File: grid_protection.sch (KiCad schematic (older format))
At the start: 10 parts, among them U2 74HC14, U6 NE555D, U7 74HC08

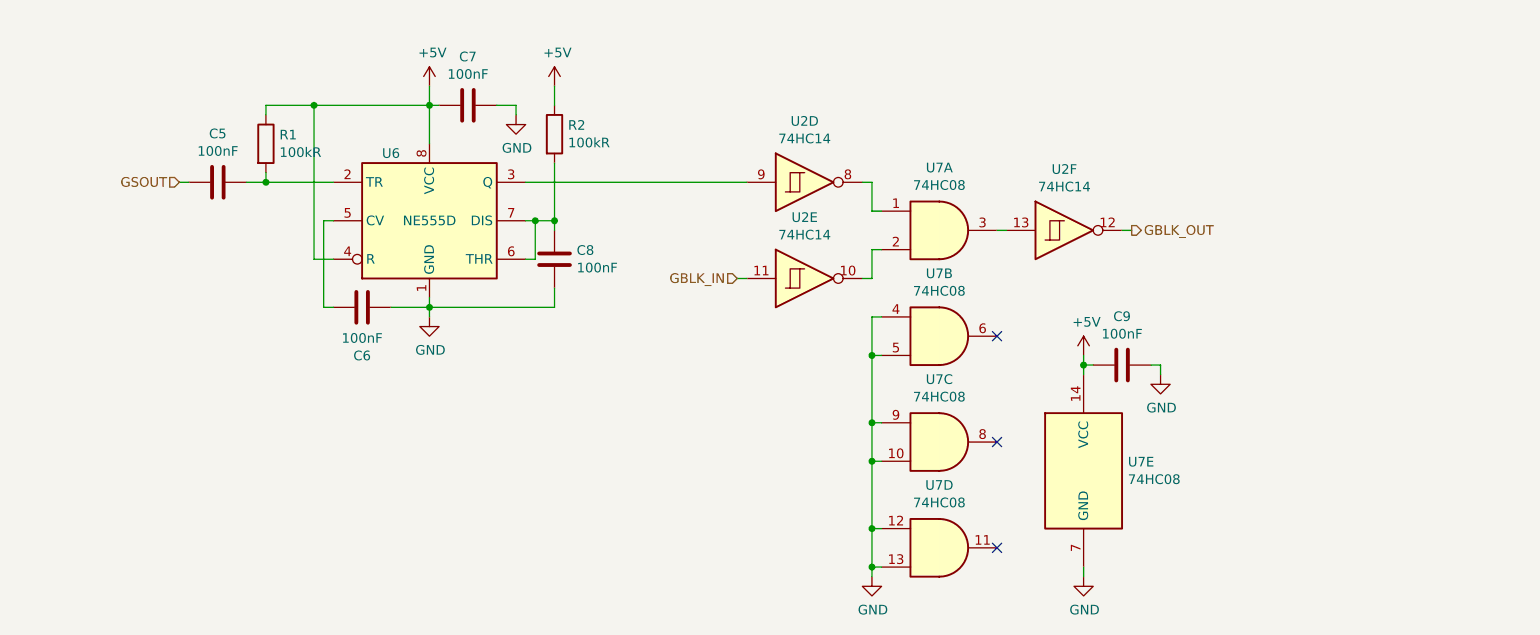
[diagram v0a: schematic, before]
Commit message: Connect shutdown and ifsel
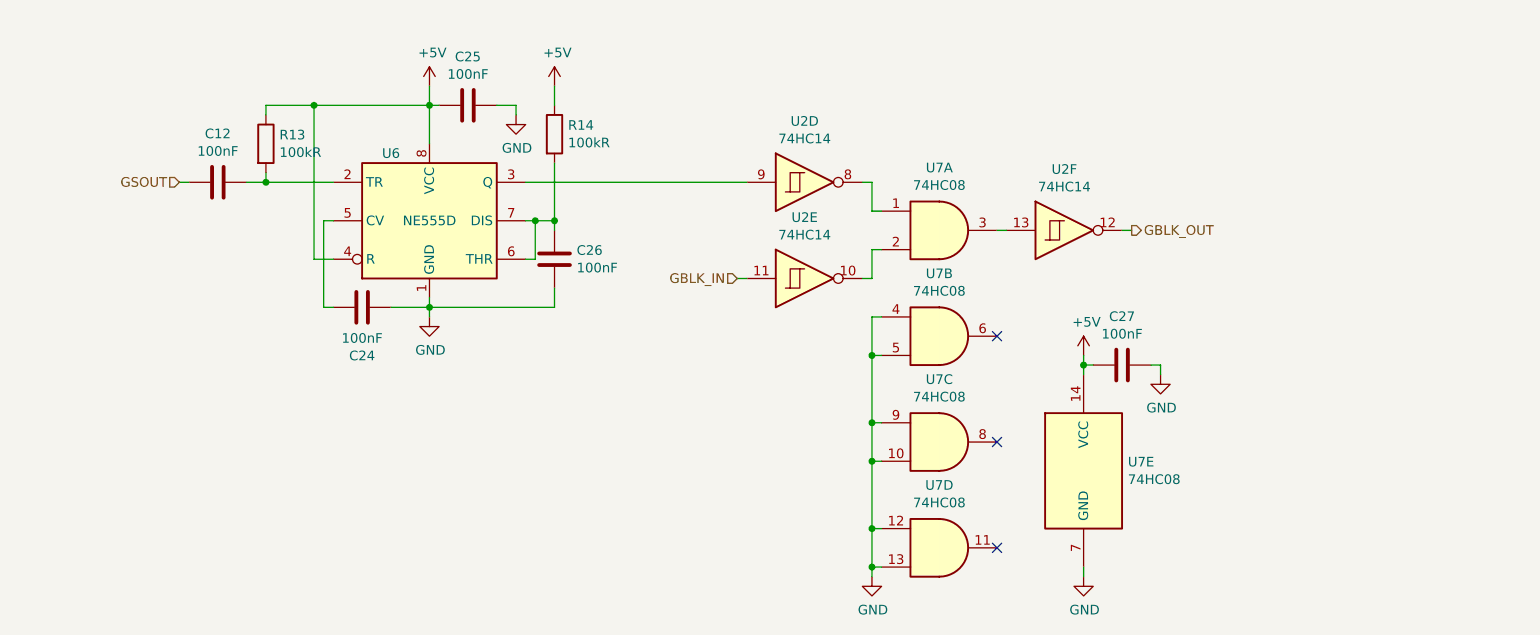
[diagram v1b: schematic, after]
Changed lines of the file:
@@
 $Descr A4 11693 8268
 encoding utf-8
-Sheet 2 4
+Sheet 4 6
 Title ""
 Date ""
@@
 AR Path="/5FBC6E69" Ref="C?"  Part="1"
 AR Path="/5FBBCA4E/5FBC6E69" Ref="C5"  Part="1"
-F 0 "C5" V 1448 3300 50  0000 C CNN
+AR Path="/60B03476/60B1C00D/5FBC6E69" Ref="C12"  Part="1"
+F 0 "C12" V 1448 3300 50  0000 C CNN
 F 1 "100nF" V 1539 3300 50  0000 C CNN
 F 2 "Capacitor_SMD:C_0402_1005Metric" H 1738 3150 50  0001 C CNN
@@
 U 1 1 5FBC8F6E
 P 2800 4000
-F 0 "#PWR014" H 2800 3750 50  0001 C CNN
+AR Path="/5FBBCA4E/5FBC8F6E" Ref="#PWR014"  Part="1"
+AR Path="/60B03476/60B1C00D/5FBC8F6E" Ref="#PWR0143"  Part="1"
+F 0 "#PWR0143" H 2800 3750 50  0001 C CNN
 F 1 "GND" H 2805 3827 50  0000 C CNN
 F 2 "" H 2800 4000 50  0001 C CNN
@@
 U 1 1 5FBC9E40
 P 3250 2950
-F 0 "#PWR015" H 3250 2700 50  0001 C CNN
+AR Path="/5FBBCA4E/5FBC9E40" Ref="#PWR015"  Part="1"
+AR Path="/60B03476/60B1C00D/5FBC9E40" Ref="#PWR0144"  Part="1"
+F 0 "#PWR0144" H 3250 2700 50  0001 C CNN
 F 1 "GND" H 3255 2777 50  0000 C CNN
 F 2 "" H 3250 2950 50  0001 C CNN
@@
 U 1 1 5FBCADA0
 P 2800 2800
-F 0 "#PWR013" H 2800 2650 50  0001 C CNN
+AR Path="/5FBBCA4E/5FBCADA0" Ref="#PWR013"  Part="1"
+AR Path="/60B03476/60B1C00D/5FBCADA0" Ref="#PWR0145"  Part="1"
+F 0 "#PWR0145" H 2800 2650 50  0001 C CNN
 F 1 "+5V" H 2815 2973 50  0000 C CNN
 F 2 "" H 2800 2800 50  0001 C CNN
@@
 AR Path="/5FBCDE60" Ref="C?"  Part="1"
 AR Path="/5FBBCA4E/5FBCDE60" Ref="C6"  Part="1"
-F 0 "C6" V 2198 3950 50  0000 C CNN
+AR Path="/60B03476/60B1C00D/5FBCDE60" Ref="C24"  Part="1"
+F 0 "C24" V 2198 3950 50  0000 C CNN
 F 1 "100nF" V 2289 3950 50  0000 C CNN
 F 2 "Capacitor_SMD:C_0402_1005Metric" H 2488 3800 50  0001 C CNN
@@
 AR Path="/5FBD22E7" Ref="C?"  Part="1"
 AR Path="/5FBBCA4E/5FBD22E7" Ref="C8"  Part="1"
-F 0 "C8" H 3565 3746 50  0000 L CNN
+AR Path="/60B03476/60B1C00D/5FBD22E7" Ref="C26"  Part="1"
+F 0 "C26" H 3565 3746 50  0000 L CNN
 F 1 "100nF" H 3565 3655 50  0000 L CNN
 F 2 "Capacitor_SMD:C_0402_1005Metric" H 3488 3550 50  0001 C CNN
@@
 U 1 1 5FBD37F0
 P 3450 3050
-F 0 "R2" H 3520 3096 50  0000 L CNN
+AR Path="/5FBBCA4E/5FBD37F0" Ref="R2"  Part="1"
+AR Path="/60B03476/60B1C00D/5FBD37F0" Ref="R14"  Part="1"
+F 0 "R14" H 3520 3096 50  0000 L CNN
 F 1 "100kR" H 3520 3005 50  0000 L CNN
 F 2 "Resistor_SMD:R_0402_1005Metric" V 3380 3050 50  0001 C CNN
@@
 U 1 1 5FBD7446
 P 3450 2800
-F 0 "#PWR016" H 3450 2650 50  0001 C CNN
+AR Path="/5FBBCA4E/5FBD7446" Ref="#PWR016"  Part="1"
+AR Path="/60B03476/60B1C00D/5FBD7446" Ref="#PWR0146"  Part="1"
+F 0 "#PWR0146" H 3450 2650 50  0001 C CNN
 F 1 "+5V" H 3465 2973 50  0000 C CNN
 F 2 "" H 3450 2800 50  0001 C CNN
@@
 U 1 1 5FBD921F
 P 1950 3100
-F 0 "R1" H 2020 3146 50  0000 L CNN
+AR Path="/5FBBCA4E/5FBD921F" Ref="R1"  Part="1"
+AR Path="/60B03476/60B1C00D/5FBD921F" Ref="R13"  Part="1"
+F 0 "R13" H 2020 3146 50  0000 L CNN
 F 1 "100kR" H 2020 3055 50  0000 L CNN
 F 2 "Resistor_SMD:R_0402_1005Metric" V 1880 3100 50  0001 C CNN
@@
 AR Path="/5FBC9A76" Ref="C?"  Part="1"
 AR Path="/5FBBCA4E/5FBC9A76" Ref="C7"  Part="1"
-F 0 "C7" V 2748 2900 50  0000 C CNN
+AR Path="/60B03476/60B1C00D/5FBC9A76" Ref="C25"  Part="1"
+F 0 "C25" V 2748 2900 50  0000 C CNN
 F 1 "100nF" V 2839 2900 50  0000 C CNN
 F 2 "Capacitor_SMD:C_0402_1005Metric" H 3038 2750 50  0001 C CNN
@@
 AR Path="/5FC1C26C" Ref="U?"  Part="4"
 AR Path="/5FBBCA4E/5FC1C26C" Ref="U7"  Part="4"
+AR Path="/60B03476/60B1C00D/5FC1C26C" Ref="U7"  Part="4"
 F 0 "U7" H 5450 5525 50  0000 C CNN
 F 1 "74HC08" H 5450 5434 50  0000 C CNN
@@
 AR Path="/5FC1C27D" Ref="C?"  Part="1"
 AR Path="/5FBBCA4E/5FC1C27D" Ref="C9"  Part="1"
-F 0 "C9" V 6148 4250 50  0000 C CNN
+AR Path="/60B03476/60B1C00D/5FC1C27D" Ref="C27"  Part="1"
+F 0 "C27" V 6148 4250 50  0000 C CNN
 F 1 "100nF" V 6239 4250 50  0000 C CNN
 F 2 "Capacitor_SMD:C_0402_1005Metric" H 6438 4100 50  0001 C CNN
@@
 AR Path="/5FC1C283" Ref="#PWR?"  Part="1"
 AR Path="/5FBBCA4E/5FC1C283" Ref="#PWR020"  Part="1"
-F 0 "#PWR020" H 6600 4050 50  0001 C CNN
+AR Path="/60B03476/60B1C00D/5FC1C283" Ref="#PWR0147"  Part="1"
+F 0 "#PWR0147" H 6600 4050 50  0001 C CNN
 F 1 "GND" H 6605 4127 50  0000 C CNN
 F 2 "" H 6600 4300 50  0001 C CNN
@@
 AR Path="/5FC1C28D" Ref="#PWR?"  Part="1"
 AR Path="/5FBBCA4E/5FC1C28D" Ref="#PWR018"  Part="1"
-F 0 "#PWR018" H 6200 4050 50  0001 C CNN
+AR Path="/60B03476/60B1C00D/5FC1C28D" Ref="#PWR0148"  Part="1"
+F 0 "#PWR0148" H 6200 4050 50  0001 C CNN
 F 1 "+5V" H 6215 4373 50  0000 C CNN
 F 2 "" H 6200 4200 50  0001 C CNN
@@
 AR Path="/5FC1C295" Ref="#PWR?"  Part="1"
 AR Path="/5FBBCA4E/5FC1C295" Ref="#PWR019"  Part="1"
-F 0 "#PWR019" H 6200 5100 50  0001 C CNN
+AR Path="/60B03476/60B1C00D/5FC1C295" Ref="#PWR0149"  Part="1"
+F 0 "#PWR0149" H 6200 5100 50  0001 C CNN
 F 1 "GND" H 6205 5177 50  0000 C CNN
 F 2 "" H 6200 5350 50  0001 C CNN
@@
 AR Path="/5FC1C29E" Ref="#PWR?"  Part="1"
 AR Path="/5FBBCA4E/5FC1C29E" Ref="#PWR017"  Part="1"
-F 0 "#PWR017" H 5100 5100 50  0001 C CNN
+AR Path="/60B03476/60B1C00D/5FC1C29E" Ref="#PWR0150"  Part="1"
+F 0 "#PWR0150" H 5100 5100 50  0001 C CNN
 F 1 "GND" H 5105 5177 50  0000 C CNN
 F 2 "" H 5100 5350 50  0001 C CNN
@@
 AR Path="/5FC1C273" Ref="U?"  Part="5"
 AR Path="/5FBBCA4E/5FC1C273" Ref="U7"  Part="5"
+AR Path="/60B03476/60B1C00D/5FC1C273" Ref="U7"  Part="5"
 F 0 "U7" H 6430 4846 50  0000 L CNN
 F 1 "74HC08" H 6430 4755 50  0000 L CNN
@@
 AR Path="/5FC1C265" Ref="U?"  Part="3"
 AR Path="/5FBBCA4E/5FC1C265" Ref="U7"  Part="3"
+AR Path="/60B03476/60B1C00D/5FC1C265" Ref="U7"  Part="3"
 F 0 "U7" H 5450 4975 50  0000 C CNN
 F 1 "74HC08" H 5450 4884 50  0000 C CNN
@@
 AR Path="/5FC1C25E" Ref="U?"  Part="2"
 AR Path="/5FBBCA4E/5FC1C25E" Ref="U7"  Part="2"
+AR Path="/60B03476/60B1C00D/5FC1C25E" Ref="U7"  Part="2"
 F 0 "U7" H 5450 4425 50  0000 C CNN
 F 1 "74HC08" H 5450 4334 50  0000 C CNN
@@
 AR Path="/5FBBEE91" Ref="U?"  Part="5"
 AR Path="/5FBBCA4E/5FBBEE91" Ref="U2"  Part="5"
+AR Path="/60B03476/60B1C00D/5FBBEE91" Ref="U2"  Part="5"
 F 0 "U2" H 4750 4117 50  0000 C CNN
 F 1 "74HC14" H 4750 4026 50  0000 C CNN
@@
 AR Path="/5FBBEE8A" Ref="U?"  Part="6"
 AR Path="/5FBBCA4E/5FBBEE8A" Ref="U2"  Part="6"
+AR Path="/60B03476/60B1C00D/5FBBEE8A" Ref="U2"  Part="6"
 F 0 "U2" H 6100 3867 50  0000 C CNN
 F 1 "74HC14" H 6100 3776 50  0000 C CNN
@@
 AR Path="/5FBBEE83" Ref="U?"  Part="1"
 AR Path="/5FBBCA4E/5FBBEE83" Ref="U7"  Part="1"
+AR Path="/60B03476/60B1C00D/5FBBEE83" Ref="U7"  Part="1"
 F 0 "U7" H 5450 3875 50  0000 C CNN
 F 1 "74HC08" H 5450 3784 50  0000 C CNN
@@
 AR Path="/5FBBEE98" Ref="U?"  Part="4"
 AR Path="/5FBBCA4E/5FBBEE98" Ref="U2"  Part="4"
+AR Path="/60B03476/60B1C00D/5FBBEE98" Ref="U2"  Part="4"
 F 0 "U2" H 4750 3617 50  0000 C CNN
 F 1 "74HC14" H 4750 3526 50  0000 C CNN
@@
 U 1 1 5FCFCDB6
 P 2800 3500
+AR Path="/5FBBCA4E/5FCFCDB6" Ref="U6"  Part="1"
+AR Path="/60B03476/60B1C00D/5FCFCDB6" Ref="U6"  Part="1"
 F 0 "U6" H 2600 3850 50  0000 C CNN
 F 1 "NE555D" H 2800 3500 50  0000 C CNN

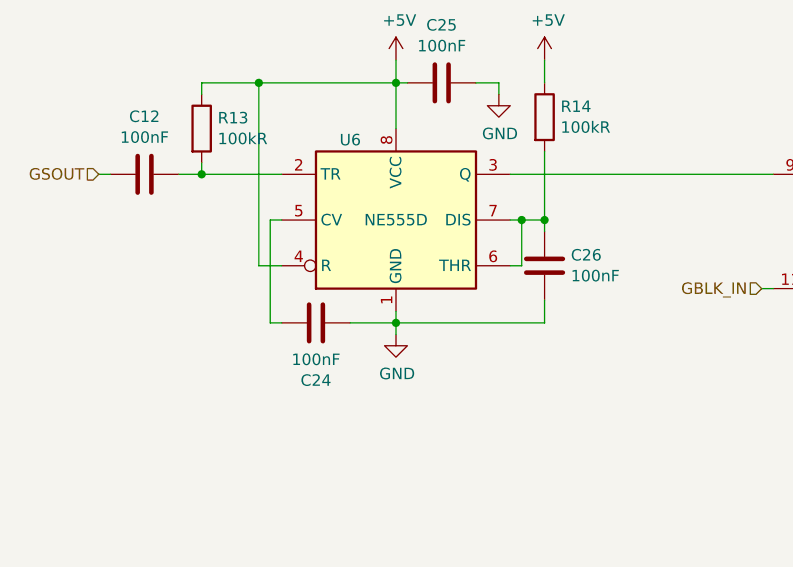
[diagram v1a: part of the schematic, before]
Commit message: Add VFD section
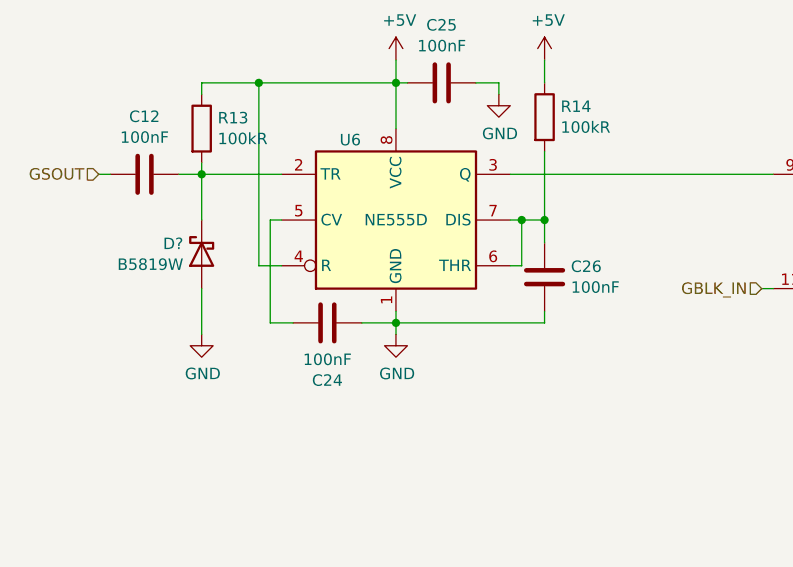
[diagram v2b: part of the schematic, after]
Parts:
- added D?: B5819W, Diode_SMD:D_SOD-123, symbol Device:D_Schottky
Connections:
- net GND: now also D?.2 (A)
- net at C5.1, R1.2, U6.2 (TR): now also D?.1 (K)
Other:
- moved on the sheet: C24, C26
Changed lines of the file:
@@
 $Descr A4 11693 8268
 encoding utf-8
-Sheet 4 6
+Sheet 4 7
 Title ""
 Date ""
@@
 L Device:C C?
 U 1 1 5FBCDE60
-P 2450 3950
+P 2500 3950
 AR Path="/5FBCDE60" Ref="C?"  Part="1"
 AR Path="/5FBBCA4E/5FBCDE60" Ref="C6"  Part="1"
 AR Path="/60B03476/60B1C00D/5FBCDE60" Ref="C24"  Part="1"
-F 0 "C24" V 2198 3950 50  0000 C CNN
-F 1 "100nF" V 2289 3950 50  0000 C CNN
-F 2 "Capacitor_SMD:C_0402_1005Metric" H 2488 3800 50  0001 C CNN
-F 3 "~" H 2450 3950 50  0001 C CNN
-F 4 "C1525" V 2450 3950 50  0001 C CNN "LCSC"
-	1    2450 3950
+F 0 "C24" V 2248 3950 50  0000 C CNN
+F 1 "100nF" V 2339 3950 50  0000 C CNN
+F 2 "Capacitor_SMD:C_0402_1005Metric" H 2538 3800 50  0001 C CNN
+F 3 "~" H 2500 3950 50  0001 C CNN
+F 4 "C1525" V 2500 3950 50  0001 C CNN "LCSC"
+	1    2500 3950
 	0    -1   -1   0
 $EndComp
 Wire Wire Line
 	2800 3900 2800 3950
-Wire Wire Line
-	2800 3950 2600 3950
 Connection ~ 2800 3950
 Wire Wire Line
 	2800 3950 2800 4000
-Wire Wire Line
-	2300 3950 2250 3950
 Wire Wire Line
 	1850 3300 1950 3300
@@
 L Device:C C?
 U 1 1 5FBD22E7
-P 3450 3700
+P 3450 3750
 AR Path="/5FBD22E7" Ref="C?"  Part="1"
 AR Path="/5FBBCA4E/5FBD22E7" Ref="C8"  Part="1"
 AR Path="/60B03476/60B1C00D/5FBD22E7" Ref="C26"  Part="1"
-F 0 "C26" H 3565 3746 50  0000 L CNN
-F 1 "100nF" H 3565 3655 50  0000 L CNN
-F 2 "Capacitor_SMD:C_0402_1005Metric" H 3488 3550 50  0001 C CNN
-F 3 "~" H 3450 3700 50  0001 C CNN
-F 4 "C1525" V 3450 3700 50  0001 C CNN "LCSC"
-	1    3450 3700
+F 0 "C26" H 3565 3796 50  0000 L CNN
+F 1 "100nF" H 3565 3705 50  0000 L CNN
+F 2 "Capacitor_SMD:C_0402_1005Metric" H 3488 3600 50  0001 C CNN
+F 3 "~" H 3450 3750 50  0001 C CNN
+F 4 "C1525" V 3450 3750 50  0001 C CNN "LCSC"
+	1    3450 3750
 	1    0    0    -1
 $EndComp
@@
 	3450 3500 3450 3200
 Connection ~ 3350 3500
-Wire Wire Line
-	3450 3500 3450 3550
 Connection ~ 3450 3500
-Wire Wire Line
-	3450 3950 3450 3850
 Wire Wire Line
 	2800 3950 3450 3950
@@
 	1    0    0    -1
 $EndComp
+$Comp
+L Device:D_Schottky D?
+U 1 1 6188A910
+P 1950 3650
+AR Path="/60B03476/60B1C0DE/6188A910" Ref="D?"  Part="1"
+AR Path="/60B03476/60B1C0E2/6188A910" Ref="D?"  Part="1"
+AR Path="/60B03476/6147410E/6188A910" Ref="D?"  Part="1"
+AR Path="/60B03476/60B1C00D/6188A910" Ref="D?"  Part="1"
+F 0 "D?" V 1904 3730 50  0000 L CNN
+F 1 "B5819W" V 1995 3730 50  0000 L CNN
+F 2 "Diode_SMD:D_SOD-123" H 1950 3650 50  0001 C CNN
+F 3 "~" H 1950 3650 50  0001 C CNN
+F 4 "C8598" H 1950 3650 50  0001 C CNN "LCSC"
+	1    1950 3650
+	0    -1   1    0
+$EndComp
+$Comp
+L power:GND #PWR?
+U 1 1 6188C155
+P 1950 4000
+F 0 "#PWR?" H 1950 3750 50  0001 C CNN
+F 1 "GND" H 1955 3827 50  0000 C CNN
+F 2 "" H 1950 4000 50  0001 C CNN
+F 3 "" H 1950 4000 50  0001 C CNN
+	1    1950 4000
+	1    0    0    -1
+$EndComp
+Wire Wire Line
+	1950 3500 1950 3300
+Wire Wire Line
+	1950 3800 1950 4000
+Wire Wire Line
+	3450 3500 3450 3600
+Wire Wire Line
+	3450 3900 3450 3950
+Wire Wire Line
+	2650 3950 2800 3950
+Wire Wire Line
+	2250 3950 2350 3950
 $EndSCHEMATC

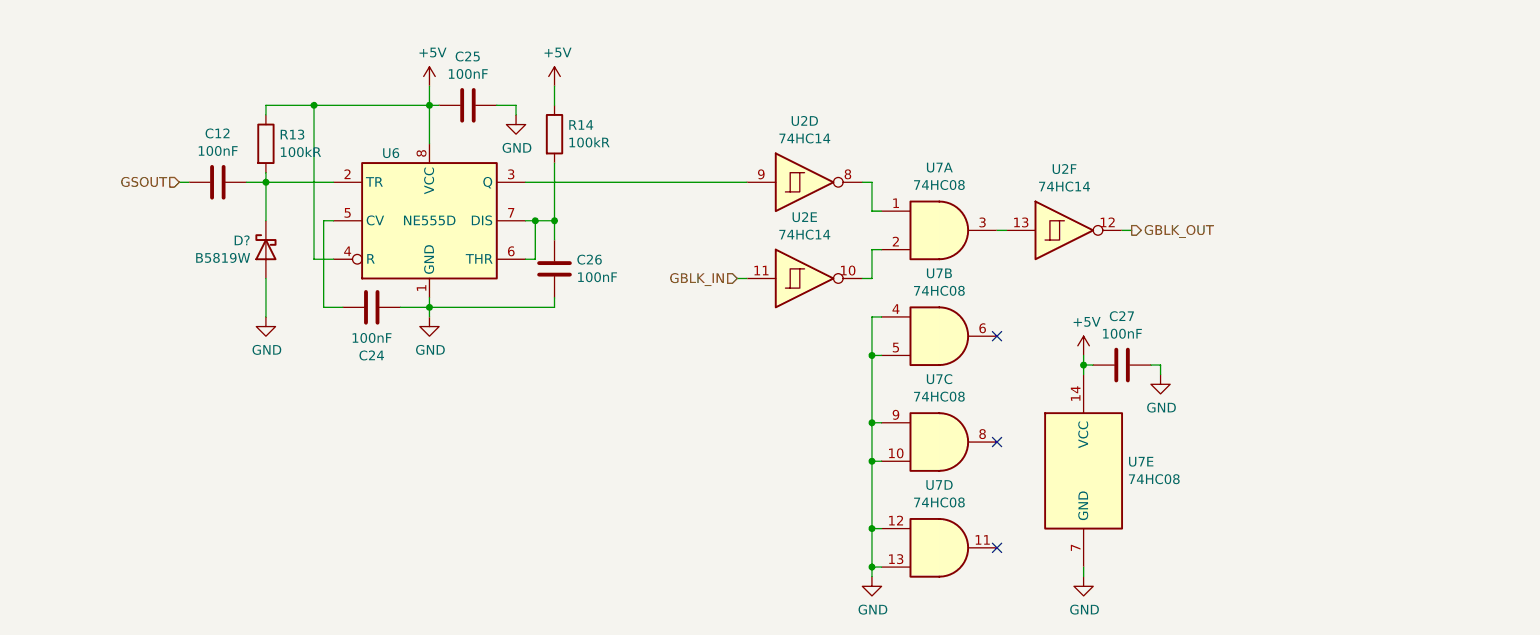
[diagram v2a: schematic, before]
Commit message: Fix grid protection
Ensure only edges are detected
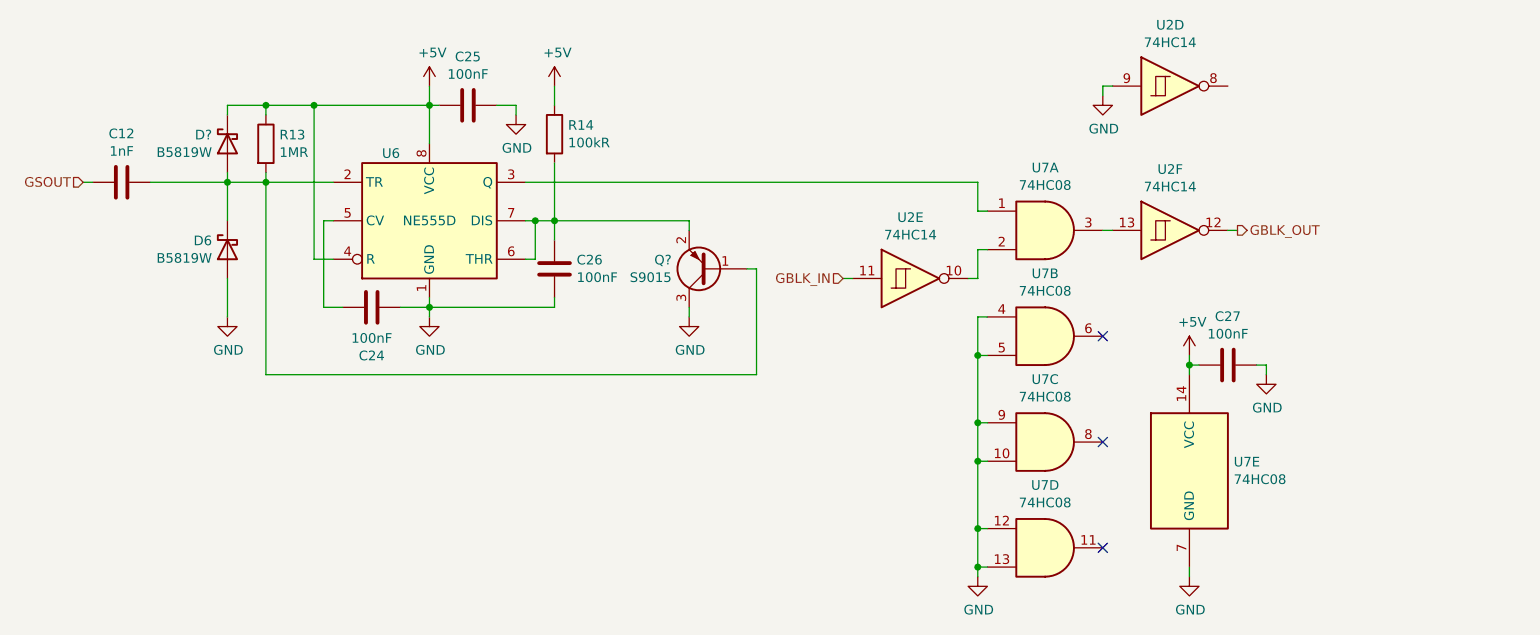
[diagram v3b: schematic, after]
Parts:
- added D?: B5819W, Diode_SMD:D_SOD-123, symbol Device:D_Schottky
- added Q?: S9015, Package_TO_SOT_SMD:SOT-23, symbol Transistor_BJT:MMBT3906
- C5: value 100nF -> 1nF; LCSC C1525 -> C1523
- R1: value 100kR -> 1MR; LCSC C25741 -> C26083
- gave numbers to parts that had none: 1
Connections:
- net +5V: now also D?.1 (K)
- net GND: now also U2.9, Q?.3 (C)
- net at U7.1: now also U6.3 (Q); no longer U2.8
- net at C5.1, D6.1 (K), R1.2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: now also D?.2 (A), Q?.1 (B)
- net at C8.1, R2.2, U6.6 (THR)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: now also Q?.2 (E)
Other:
- moved on the sheet: C12, C27, D6, U2D, U2E, U2F, U7A, U7B, U7C, U7D, U7E

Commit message: Complete intra section layout
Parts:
- removed D6: B5819W, Diode_SMD:D_SOD-123, symbol Device:D_Schottky
- added R42: 50R, Resistor_SMD:R_0402_1005Metric, symbol Device:R
- gave numbers to parts that had none: 2
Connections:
- net GSOUT: now also R42.2; no longer C5.2
- new net: C5.2, R42.1
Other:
- moved on the sheet: C12, C24, C25, C26, C27, D7, Q18, R13, R14, U2D, U2E, U2F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
